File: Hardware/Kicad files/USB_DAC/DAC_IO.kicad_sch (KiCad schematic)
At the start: 11 parts, among them J1 NC3MAH, J10 B4B-PH-K-S, J3 B7B-PH-K-S, J5 Jack-DC, J7 B2B-PH-K-S, J8 NC3MAH, J9 USB4110GFA, U3 IP4234CZ6

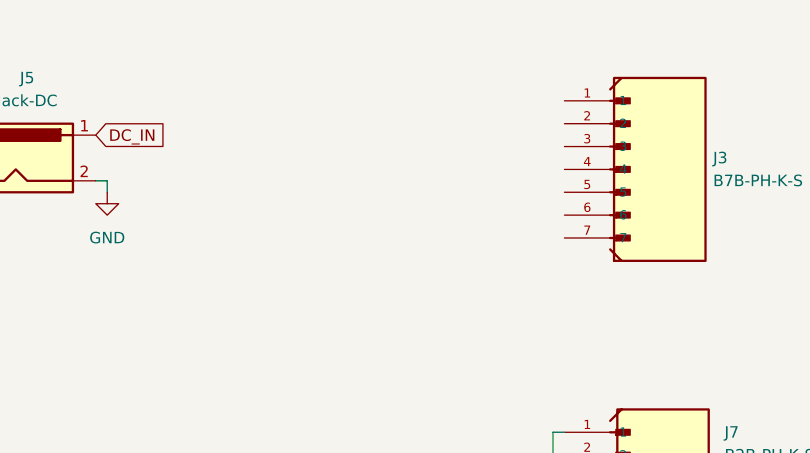
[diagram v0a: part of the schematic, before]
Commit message: added STM code files and modified PCB
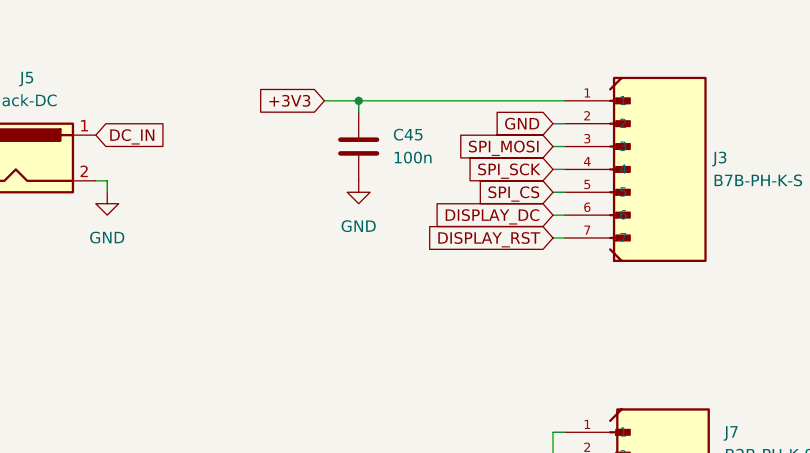
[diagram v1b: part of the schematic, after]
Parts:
- added C45: 100n, Capacitor_SMD:C_0603_1608Metric, symbol Device:C
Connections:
- net GND: now also J3.2, C45.2
- net +3V3: now reaches J3.1
- net +3V3: now also C45.1
- net SPI_MOSI: now reaches J3.3
- net SPI_SCK: now reaches J3.4
- net SPI_CS: now reaches J3.5
- net DISPLAY_DC: now reaches J3.6
- net DISPLAY_RST: now reaches J3.7

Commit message: Updated PCB and schematics
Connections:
- net DC_IN: now also J7.1
- net GND: now also J7.2
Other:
- note added: "Button and LED"
- note added: "DC input"
- note added: "Display"
- note added: "Inputs and outputs"
- note added: "USB-C connector"
- note added: "XLR outputs"
- note removed: "- DISPLAY (7Pins) - USB-C - RCA / XLR OUTPUT - PWR button"
- company: (none) -> Linus Fridlund
- title: (none) -> I/O Sheet
- moved on the sheet: C45, J1, J10, J3, J5, J7, J8, J9, R18, R4, R5, U3
